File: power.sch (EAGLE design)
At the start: 24 parts

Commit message: I'm starting to like this layout.  Not sure why.
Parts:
- added H2, H3: MOUNT-PAD-ROUND2.8, holes:MOUNT-PAD-ROUND2.8
- added R7: 15k, rcl:R-US_R0603
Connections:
- net GND: now also H2.MOUNT, H3.MOUNT
- net N$10: now also R7.2, U$6.AIN0; no longer U$6.AIN2
- net N$12: now also U$6.AIN2; no longer U$6.AIN0
- net N$7: now also R7.1
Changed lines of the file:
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@@
 <part name="U$7" library="semiconductors" deviceset="45NO6LG" device=""/>
 <part name="U$8" library="semiconductors" deviceset="45NO6LG" device=""/>
+<part name="H2" library="holes" deviceset="MOUNT-PAD-ROUND" device="2.8"/>
+<part name="H3" library="holes" deviceset="MOUNT-PAD-ROUND" device="2.8"/>
+<part name="R7" library="rcl" deviceset="R-US_" device="R0603" value="15k"/>
 </parts>
 <sheets>
@@
 <instance part="U$7" gate="G$1" x="22.86" y="17.78"/>
 <instance part="U$8" gate="G$1" x="40.64" y="17.78"/>
+<instance part="H2" gate="G$1" x="83.82" y="71.12"/>
+<instance part="H3" gate="G$1" x="83.82" y="81.28"/>
+<instance part="R7" gate="G$1" x="66.04" y="25.4" rot="R180"/>
 </instances>
 <busses>
@@
 <wire x1="81.28" y1="71.12" x2="78.74" y2="71.12" width="0.1524" layer="91"/>
 <junction x="78.74" y="71.12"/>
+<pinref part="H2" gate="G$1" pin="MOUNT"/>
+<pinref part="H3" gate="G$1" pin="MOUNT"/>
+<wire x1="81.28" y1="81.28" x2="78.74" y2="81.28" width="0.1524" layer="91"/>
+<wire x1="78.74" y1="81.28" x2="78.74" y2="76.2" width="0.1524" layer="91"/>
+<junction x="78.74" y="76.2"/>
 </segment>
 </net>
@@
 <junction x="76.2" y="58.42"/>
 <pinref part="BAT+" gate="G$1" pin="MOUNT"/>
+<pinref part="R7" gate="G$1" pin="1"/>
 </segment>
 </net>
@@
 <net name="N$10" class="0">
 <segment>
-<pinref part="U$6" gate="G$1" pin="AIN2"/>
-<wire x1="88.9" y1="-30.48" x2="124.46" y2="-30.48" width="0.1524" layer="91"/>
-<wire x1="88.9" y1="-33.02" x2="88.9" y2="-30.48" width="0.1524" layer="91"/>
-<wire x1="68.58" y1="-33.02" x2="88.9" y2="-33.02" width="0.1524" layer="91"/>
-<wire x1="68.58" y1="-25.4" x2="68.58" y2="-33.02" width="0.1524" layer="91"/>
 <pinref part="R8" gate="G$1" pin="2"/>
 <wire x1="60.96" y1="25.4" x2="60.96" y2="20.32" width="0.1524" layer="91"/>
@@
 <wire x1="60.96" y1="20.32" x2="58.42" y2="20.32" width="0.1524" layer="91"/>
 <wire x1="58.42" y1="20.32" x2="58.42" y2="-25.4" width="0.1524" layer="91"/>
-<wire x1="58.42" y1="-25.4" x2="68.58" y2="-25.4" width="0.1524" layer="91"/>
-</segment>
-</net>
-<net name="N$12" class="0">
-<segment>
+<wire x1="58.42" y1="-25.4" x2="66.04" y2="-25.4" width="0.1524" layer="91"/>
+<pinref part="R7" gate="G$1" pin="2"/>
 <pinref part="U$6" gate="G$1" pin="AIN0"/>
 <wire x1="91.44" y1="-33.02" x2="124.46" y2="-33.02" width="0.1524" layer="91"/>
 <wire x1="91.44" y1="-35.56" x2="91.44" y2="-33.02" width="0.1524" layer="91"/>
 <wire x1="66.04" y1="-35.56" x2="91.44" y2="-35.56" width="0.1524" layer="91"/>
-<wire x1="66.04" y1="-33.02" x2="66.04" y2="-35.56" width="0.1524" layer="91"/>
-<wire x1="-25.4" y1="-33.02" x2="66.04" y2="-33.02" width="0.1524" layer="91"/>
+<wire x1="66.04" y1="-25.4" x2="66.04" y2="-35.56" width="0.1524" layer="91"/>
+</segment>
+</net>
+<net name="N$12" class="0">
+<segment>
+<wire x1="-25.4" y1="-33.02" x2="88.9" y2="-33.02" width="0.1524" layer="91"/>
 <pinref part="R4" gate="G$1" pin="2"/>
 <pinref part="R3" gate="G$1" pin="2"/>
@@
 <wire x1="-7.62" y1="27.94" x2="-25.4" y2="27.94" width="0.1524" layer="91"/>
 <wire x1="-25.4" y1="27.94" x2="-25.4" y2="-33.02" width="0.1524" layer="91"/>
-</segment>
-</net>
+<pinref part="U$6" gate="G$1" pin="AIN2"/>
+<wire x1="88.9" y1="-30.48" x2="124.46" y2="-30.48" width="0.1524" layer="91"/>
+<wire x1="88.9" y1="-33.02" x2="88.9" y2="-30.48" width="0.1524" layer="91"/>
+</segment>
+</net>

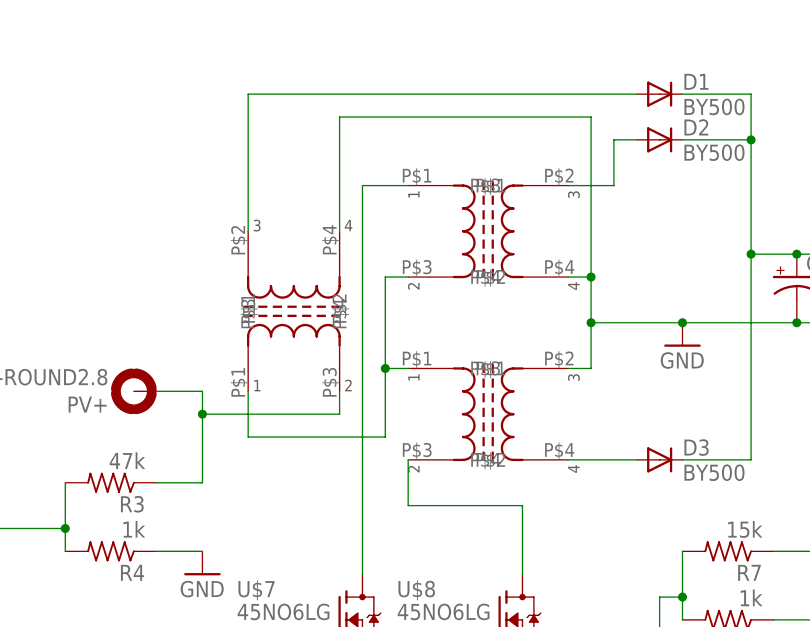
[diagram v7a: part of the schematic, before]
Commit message: Corrected choke packages in library
Rerouted board to reflect library changes
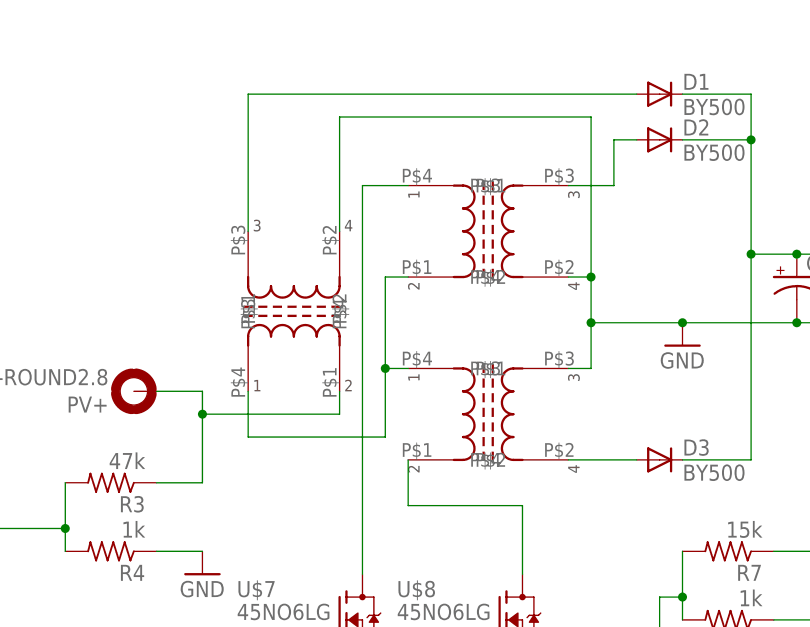
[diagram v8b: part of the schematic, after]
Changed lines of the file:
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@@
 <?xml version="1.0" encoding="utf-8"?>
 <!DOCTYPE eagle SYSTEM "eagle.dtd">
-<eagle version="6.5.0">
+<eagle version="6.5.1">
 <drawing>
 <settings>
@@
 <grid distance="0.1" unitdist="inch" unit="inch" style="lines" multiple="1" display="no" altdistance="0.01" altunitdist="inch" altunit="inch"/>
 <layers>
-<layer number="1" name="Top" color="4" fill="1" visible="yes" active="no"/>
-<layer number="16" name="Bottom" color="1" fill="1" visible="yes" active="no"/>
-<layer number="17" name="Pads" color="2" fill="1" visible="yes" active="no"/>
-<layer number="18" name="Vias" color="2" fill="1" visible="yes" active="no"/>
-<layer number="19" name="Unrouted" color="6" fill="1" visible="yes" active="no"/>
-<layer number="20" name="Dimension" color="15" fill="1" visible="yes" active="no"/>
-<layer number="21" name="tPlace" color="7" fill="1" visible="yes" active="no"/>
-<layer number="22" name="bPlace" color="7" fill="1" visible="yes" active="no"/>
-<layer number="23" name="tOrigins" color="15" fill="1" visible="yes" active="no"/>
-<layer number="24" name="bOrigins" color="15" fill="1" visible="yes" active="no"/>
-<layer number="25" name="tNames" color="7" fill="1" visible="yes" active="no"/>
-<layer number="26" name="bNames" color="7" fill="1" visible="yes" active="no"/>
-<layer number="27" name="tValues" color="7" fill="1" visible="yes" active="no"/>
-<layer number="28" name="bValues" color="7" fill="1" visible="yes" active="no"/>
+<layer number="1" name="Top" color="4" fill="1" visible="no" active="no"/>
+<layer number="16" name="Bottom" color="1" fill="1" visible="no" active="no"/>
+<layer number="17" name="Pads" color="2" fill="1" visible="no" active="no"/>
+<layer number="18" name="Vias" color="2" fill="1" visible="no" active="no"/>
+<layer number="19" name="Unrouted" color="6" fill="1" visible="no" active="no"/>
+<layer number="20" name="Dimension" color="15" fill="1" visible="no" active="no"/>
+<layer number="21" name="tPlace" color="7" fill="1" visible="no" active="no"/>
+<layer number="22" name="bPlace" color="7" fill="1" visible="no" active="no"/>
+<layer number="23" name="tOrigins" color="15" fill="1" visible="no" active="no"/>
+<layer number="24" name="bOrigins" color="15" fill="1" visible="no" active="no"/>
+<layer number="25" name="tNames" color="7" fill="1" visible="no" active="no"/>
+<layer number="26" name="bNames" color="7" fill="1" visible="no" active="no"/>
+<layer number="27" name="tValues" color="7" fill="1" visible="no" active="no"/>
+<layer number="28" name="bValues" color="7" fill="1" visible="no" active="no"/>
 <layer number="29" name="tStop" color="7" fill="3" visible="no" active="no"/>
 <layer number="30" name="bStop" color="7" fill="6" visible="no" active="no"/>
@@
 <layer number="35" name="tGlue" color="7" fill="4" visible="no" active="no"/>
 <layer number="36" name="bGlue" color="7" fill="5" visible="no" active="no"/>
-<layer number="37" name="tTest" color="7" fill="1" visible="yes" active="no"/>
-<layer number="38" name="bTest" color="7" fill="1" visible="yes" active="no"/>
+<layer number="37" name="tTest" color="7" fill="1" visible="no" active="no"/>
+<layer number="38" name="bTest" color="7" fill="1" visible="no" active="no"/>
 <layer number="39" name="tKeepout" color="4" fill="11" visible="no" active="no"/>
 <layer number="40" name="bKeepout" color="1" fill="11" visible="no" active="no"/>
@@
 <layer number="44" name="Drills" color="7" fill="1" visible="no" active="no"/>
 <layer number="45" name="Holes" color="7" fill="1" visible="no" active="no"/>
-<layer number="46" name="Milling" color="3" fill="1" visible="yes" active="no"/>
-<layer number="47" name="Measures" color="7" fill="1" visible="yes" active="no"/>
-<layer number="48" name="Document" color="7" fill="1" visible="yes" active="no"/>
-<layer number="49" name="Reference" color="7" fill="1" visible="yes" active="no"/>
-<layer number="50" name="dxf" color="7" fill="1" visible="yes" active="no"/>
-<layer number="51" name="tDocu" color="7" fill="1" visible="yes" active="no"/>
-<layer number="52" name="bDocu" color="7" fill="1" visible="yes" active="no"/>
-<layer number="53" name="tGND_GNDA" color="7" fill="9" visible="yes" active="no"/>
-<layer number="54" name="bGND_GNDA" color="1" fill="9" visible="yes" active="no"/>
-<layer number="56" name="wert" color="7" fill="1" visible="yes" active="no"/>
-<layer number="57" name="tCAD" color="7" fill="1" visible="yes" active="no"/>
+<layer number="46" name="Milling" color="3" fill="1" visible="no" active="no"/>
+<layer number="47" name="Measures" color="7" fill="1" visible="no" active="no"/>
+<layer number="48" name="Document" color="7" fill="1" visible="no" active="no"/>
+<layer number="49" name="Reference" color="7" fill="1" visible="no" active="no"/>
+<layer number="50" name="dxf" color="7" fill="1" visible="no" active="no"/>
+<layer number="51" name="tDocu" color="7" fill="1" visible="no" active="no"/>
+<layer number="52" name="bDocu" color="7" fill="1" visible="no" active="no"/>
+<layer number="53" name="tGND_GNDA" color="7" fill="9" visible="no" active="no"/>
+<layer number="54" name="bGND_GNDA" color="1" fill="9" visible="no" active="no"/>
+<layer number="56" name="wert" color="7" fill="1" visible="no" active="no"/>
+<layer number="57" name="tCAD" color="7" fill="1" visible="no" active="no"/>
 <layer number="91" name="Nets" color="2" fill="1" visible="yes" active="yes"/>
 <layer number="92" name="Busses" color="1" fill="1" visible="yes" active="yes"/>
